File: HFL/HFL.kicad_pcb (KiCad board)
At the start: 2 copper layers, 62.6 x 37.6 mm, 82 parts, among them J1 STS_IO, J2 Conn_01x06_Male, J3 PWR, Q1 2N7002, Q2 MCT06P10-TP, Q3 2N7002, SW1 RST, SW2 BYPASS, U1 74LS32, U2 74LS08, U3 MCP6004, U4 LM1117-5.0, U5 4044, U6 NE555, U7 LTV-817S

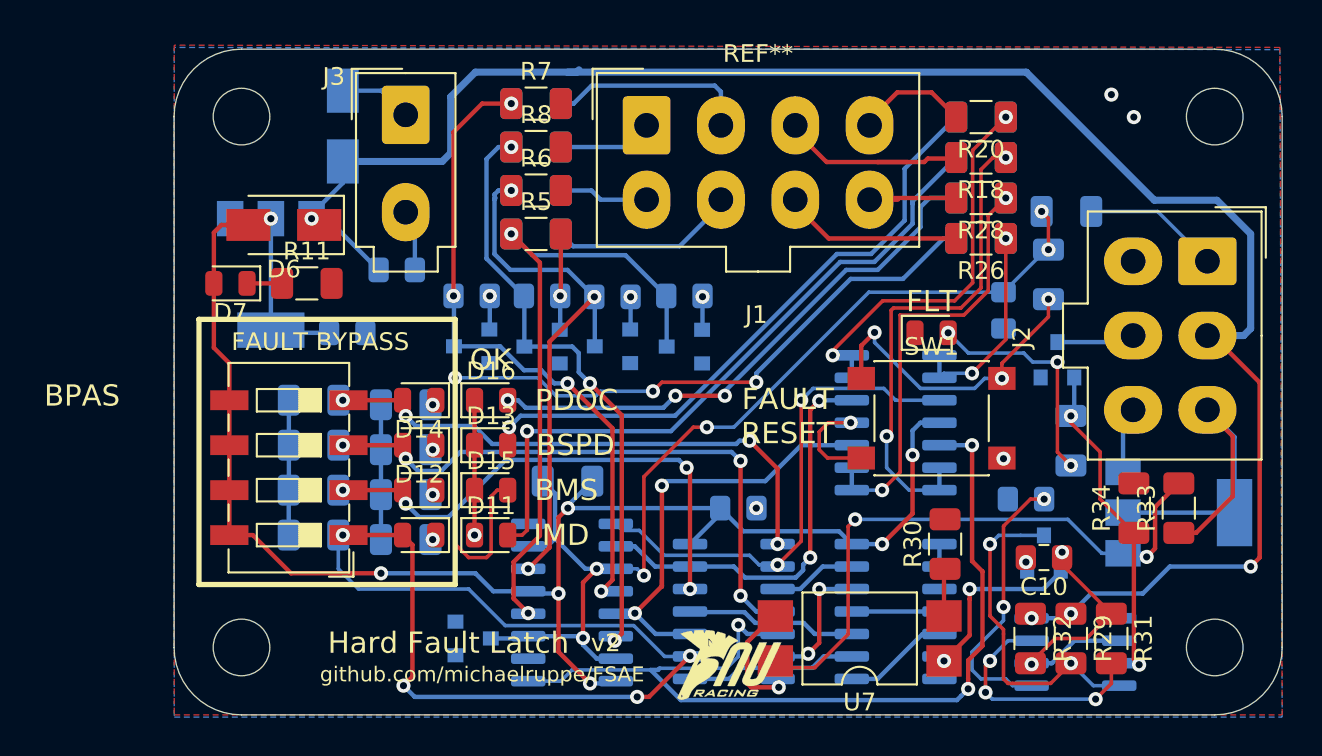
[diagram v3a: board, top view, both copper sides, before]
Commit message: Cosmetic upgrades to HFL v2
also scattered some GND-GND vias
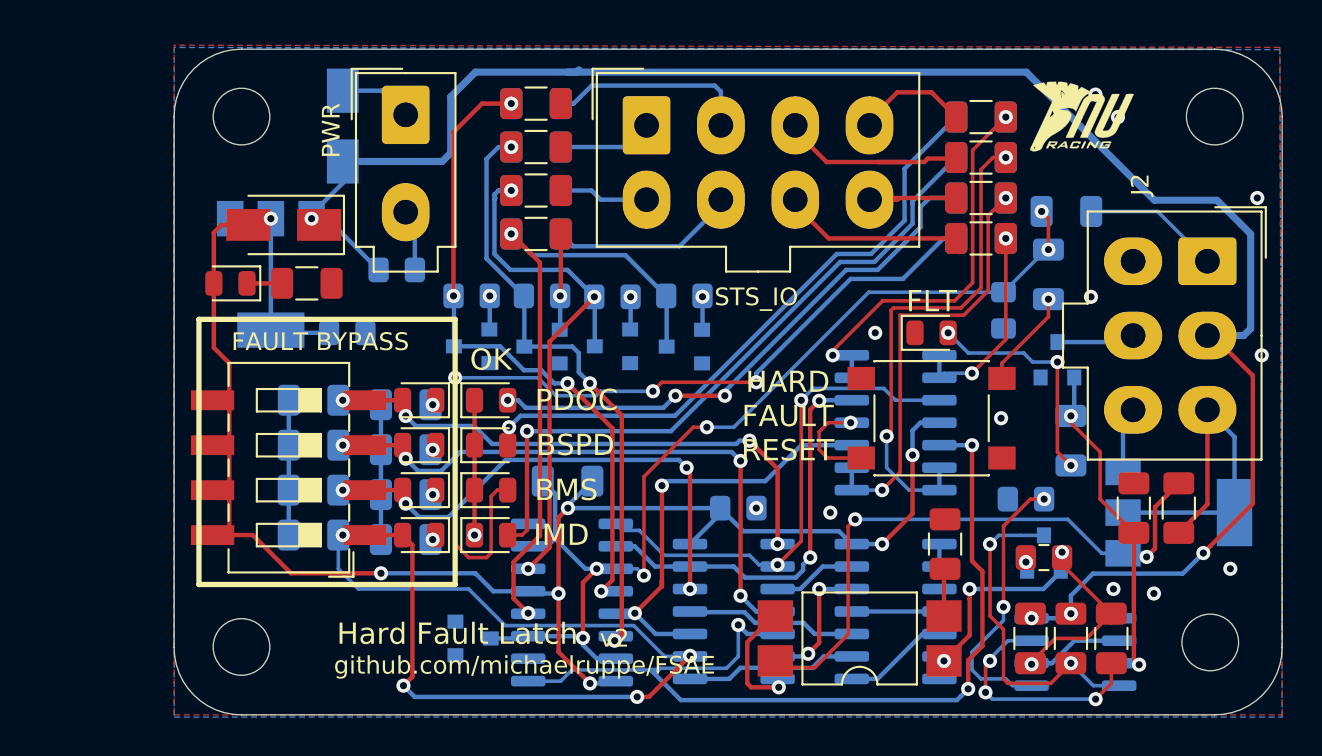
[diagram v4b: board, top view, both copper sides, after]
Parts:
- removed the REF** at (135.0, 79.5)
- removed the REF** at (80.0, 79.5)
- added REF**: MountingHole_3.2mm_M3, MountingHole:MountingHole_3.2mm_M3, F.Cu at (134.8, 79.2)
- added REF**: MountingHole_3.2mm_M3, MountingHole:MountingHole_3.2mm_M3, F.Cu at (80.0, 79.5)
- SW2: footprint Button_Switch_SMD:SW_DIP_SPSTx04_Slide_6.7x11.72mm_W6.73mm_P2.54mm_LowProfile_JPin -> Button_Switch_SMD:SW_DIP_SPSTx04_Slide_6.7x11.72mm_W8.61mm_P2.54mm_LowProfile
- moved G*** 36.8 mm to (127.5, 49.6)
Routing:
- net Net-(R12-Pad2): track 17.6 -> 5.57 mm, vias 3 -> 1
- net SHTDN_IN: track 22.1 -> 20.4 mm
- net +12V: track 105.0 -> 103.3 mm
- net GND: vias 12 -> 20
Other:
- board text added: "HARD FAULT RESET"
- board text added: "PWR"
- board text removed: "BPAS"
- board text removed: "FAULT RESET"

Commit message: Update HFL - pcb silk
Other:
- board text added: "FAULT"
- board text added: "RESET"
- board text removed: "FLT"
- board text removed: "HARD FAULT RESET"

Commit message: Lock down before branch for projects
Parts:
- moved REF** 0.35 mm to (135.0, 79.5)
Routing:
- net +12V: track 103.0 -> 115.4 mm, vias 4 -> 3
- net Net-(Q3-Pad1): track 19.1 -> 20.9 mm
- net GND: vias 20 -> 18
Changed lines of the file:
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@@
     (thickness 1.6)
     (drawings 24)
-    (tracks 655)
+    (tracks 658)
     (zones 0)
     (modules 82)
@@
     (pad_to_mask_clearance 0.051)
     (solder_mask_min_width 0.25)
-    (aux_axis_origin 0 0)
+    (aux_axis_origin 80.01 79.53)
     (grid_origin 80.01 79.53)
     (visible_elements 7FFFFFFF)
@@
     (add_net SHTDN_OUT)
   )
-  (module MountingHole:MountingHole_3.2mm_M3 (layer F.Cu)
-    (at 134.756 79.248)
+  (module MountingHole:MountingHole_3.2mm_M3 locked (layer F.Cu)
+    (at 135 79.502)
     (descr "Mounting Hole 3.2mm, no annular, M3")
     (tags "mounting hole 3.2mm no annular m3")
@@
   )
   (module MountingHole:MountingHole_3.2mm_M3 locked (layer F.Cu)
-    (at 135.01 49.53)
+    (at 135 49.53)
     (descr "Mounting Hole 3.2mm, no annular, M3")
     (tags "mounting hole 3.2mm no annular m3")
@@
   )
   (module MountingHole:MountingHole_3.2mm_M3 locked (layer F.Cu)
-    (at 80.01 49.53)
+    (at 80 49.53)
     (descr "Mounting Hole 3.2mm, no annular, M3")
     (tags "mounting hole 3.2mm no annular m3")
@@
   (via (at 128.016 59.718) (size 0.8) (drill 0.4) (layers F.Cu B.Cu) (net 1))
   (via (at 115.824 61.75) (size 0.8) (drill 0.4) (layers F.Cu B.Cu) (net 1))
-  (via (at 131.572 76.482) (size 0.8) (drill 0.4) (layers F.Cu B.Cu) (net 1))
   (segment (start 115.033 68.826) (end 113.13 68.826) (width 0.2032) (layer F.Cu) (net 1) (status 10))
   (via (at 113.284 71.91) (size 0.8) (drill 0.4) (layers F.Cu B.Cu) (net 1))
-  (via (at 129.286 76.228) (size 0.8) (drill 0.4) (layers F.Cu B.Cu) (net 1))
-  (via (at 135.89 75.085) (size 0.8) (drill 0.4) (layers F.Cu B.Cu) (net 1))
+  (via (at 132.08 76.101) (size 0.8) (drill 0.4) (layers F.Cu B.Cu) (net 1))
   (segment (start 80.3215 58.956) (end 82.302 58.956) (width 0.25) (layer F.Cu) (net 2) (status 30))
   (via (at 90.814 73.434) (size 0.8) (drill 0.4) (layers F.Cu B.Cu) (net 3) (status 30))
@@
   (segment (start 124.661 77.879) (end 126.625 77.879) (width 0.25) (layer B.Cu) (net 4) (status 10))
   (via (at 124.661 77.879) (size 0.8) (drill 0.4) (layers F.Cu B.Cu) (net 4) (status 30))
-  (segment (start 134.765999 73.796001) (end 134.366 74.196) (width 0.25) (layer F.Cu) (net 4))
-  (segment (start 134.596 61.904) (end 134.896 61.904) (width 0.25) (layer F.Cu) (net 4))
+  (segment (start 137.16 64.168) (end 137.16 71.021) (width 0.25) (layer F.Cu) (net 4))
   (segment (start 134.896 61.904) (end 137.16 64.168) (width 0.25) (layer F.Cu) (net 4))
-  (segment (start 137.16 64.168) (end 137.16 71.402) (width 0.25) (layer F.Cu) (net 4))
-  (segment (start 137.16 71.402) (end 134.765999 73.796001) (width 0.25) (layer F.Cu) (net 4))
-  (via (at 134.366 74.196) (size 0.8) (drill 0.4) (layers F.Cu B.Cu) (net 4))
-  (segment (start 133.966001 74.595999) (end 134.366 74.196) (width 0.25) (layer B.Cu) (net 4))
-  (segment (start 133.204001 75.357999) (end 133.966001 74.595999) (width 0.25) (layer B.Cu) (net 4))
-  (segment (start 128.124001 75.357999) (end 133.204001 75.357999) (width 0.25) (layer B.Cu) (net 4))
-  (segment (start 126.882 77.622) (end 126.882 76.6) (width 0.25) (layer B.Cu) (net 4))
-  (segment (start 126.882 76.6) (end 128.124001 75.357999) (width 0.25) (layer B.Cu) (net 4))
+  (segment (start 134.596 61.904) (end 134.896 61.904) (width 0.25) (layer F.Cu) (net 4))
+  (segment (start 137.795 64.803) (end 134.896 61.904) (width 0.25) (layer B.Cu) (net 4))
+  (segment (start 128.784 75.72) (end 130.937 75.72) (width 0.25) (layer B.Cu) (net 4))
+  (segment (start 126.882 77.622) (end 128.784 75.72) (width 0.25) (layer B.Cu) (net 4))
+  (segment (start 134.896 61.904) (end 134.596 61.904) (width 0.25) (layer B.Cu) (net 4))
+  (segment (start 130.937 75.72) (end 131.953 74.704) (width 0.25) (layer B.Cu) (net 4))
+  (segment (start 131.953 74.704) (end 137.432999 74.704) (width 0.25) (layer B.Cu) (net 4))
+  (segment (start 137.432999 74.704) (end 137.795 74.341999) (width 0.25) (layer B.Cu) (net 4))
+  (segment (start 137.795 74.341999) (end 137.795 64.803) (width 0.25) (layer B.Cu) (net 4))
   (via (at 95.256 56.162) (size 0.8) (drill 0.4) (layers F.Cu B.Cu) (net 5) (status 30))
   (segment (start 104.038 59.689666) (end 104.013 59.664666) (width 0.25) (layer B.Cu) (net 5) (status 30))
@@
   (via (at 90.814 68.354) (size 0.8) (drill 0.4) (layers F.Cu B.Cu) (net 39) (status 30))
   (via (at 90.814 65.814) (size 0.8) (drill 0.4) (layers F.Cu B.Cu) (net 40) (status 30))
-  (via (at 131.16301 74.412988) (size 0.8) (drill 0.4) (layers F.Cu B.Cu) (net 41))
-  (segment (start 132.978 70.256) (end 131.63801 71.59599) (width 0.25) (layer F.Cu) (net 41) (status 10))
-  (segment (start 131.63801 71.59599) (end 131.63801 73.937988) (width 0.25) (layer F.Cu) (net 41))
-  (segment (start 131.63801 73.937988) (end 131.16301 74.412988) (width 0.25) (layer F.Cu) (net 41))
   (segment (start 128.6248 74.21) (end 126.7058 72.291) (width 0.2032) (layer B.Cu) (net 41))
   (segment (start 129.828 74.21) (end 128.6248 74.21) (width 0.2032) (layer B.Cu) (net 41) (status 10))
@@
   (segment (start 114.69 72.291) (end 114.290001 72.690999) (width 0.2032) (layer F.Cu) (net 41))
   (segment (start 114.290001 72.690999) (end 114.290001 78.786999) (width 0.2032) (layer F.Cu) (net 41))
-  (segment (start 130.960022 74.21) (end 131.16301 74.412988) (width 0.2032) (layer B.Cu) (net 41))
-  (segment (start 129.828 74.21) (end 130.960022 74.21) (width 0.2032) (layer B.Cu) (net 41) (status 10))
+  (segment (start 129.828 74.21) (end 129.860999 74.177001) (width 0.2032) (layer B.Cu) (net 41))
+  (segment (start 132.978 70.256) (end 131.699 71.535) (width 0.25) (layer F.Cu) (net 41))
+  (segment (start 129.860999 74.177001) (end 129.902001 74.177001) (width 0.2032) (layer B.Cu) (net 41))
+  (segment (start 129.902001 74.177001) (end 130.302 74.577) (width 0.2032) (layer B.Cu) (net 41))
+  (segment (start 130.867685 74.577) (end 130.302 74.577) (width 0.25) (layer F.Cu) (net 41))
+  (segment (start 131.699 73.745685) (end 130.867685 74.577) (width 0.25) (layer F.Cu) (net 41))
+  (via (at 130.302 74.577) (size 0.8) (drill 0.4) (layers F.Cu B.Cu) (net 41))
+  (segment (start 131.699 71.535) (end 131.699 73.745685) (width 0.25) (layer F.Cu) (net 41))
   (segment (start 127.07 66.258) (end 126.882 66.446) (width 0.25) (layer B.Cu) (net 42) (status 30))
   (segment (start 127.07 64.274) (end 127.07 66.258) (width 0.25) (layer B.Cu) (net 42) (status 30))
@@
   (segment (start 128.533 68.481) (end 126.882 66.83) (width 0.2032) (layer F.Cu) (net 42))
   (segment (start 126.882 66.83) (end 126.882 66.446) (width 0.2032) (layer F.Cu) (net 42))
-  (segment (start 130.438 73.056) (end 130.438 80.20591) (width 0.25) (layer F.Cu) (net 42) (status 10))
   (via (at 130.736824 80.504734) (size 0.8) (drill 0.4) (layers F.Cu B.Cu) (net 42))
-  (segment (start 130.438 80.20591) (end 130.736824 80.504734) (width 0.25) (layer F.Cu) (net 42))
   (segment (start 129.696734 80.504734) (end 129.611 80.419) (width 0.25) (layer B.Cu) (net 42) (status 30))
   (segment (start 130.736824 80.504734) (end 129.696734 80.504734) (width 0.25) (layer B.Cu) (net 42) (status 20))
+  (segment (start 130.736824 80.504734) (end 130.736824 76.465826) (width 0.25) (layer F.Cu) (net 42))
+  (segment (start 128.905 73.614) (end 129.463 73.056) (width 0.25) (layer F.Cu) (net 42))
+  (segment (start 129.463 73.056) (end 130.438 73.056) (width 0.25) (layer F.Cu) (net 42))
+  (segment (start 128.905 74.634002) (end 128.905 73.614) (width 0.25) (layer F.Cu) (net 42))
+  (segment (start 130.736824 76.465826) (end 128.905 74.634002) (width 0.25) (layer F.Cu) (net 42))
   (via (at 125.612 59.848) (size 0.8) (drill 0.4) (layers F.Cu B.Cu) (net 43) (status 30))
   (segment (start 125.612 60.8438) (end 125.612 59.848) (width 0.2032) (layer F.Cu) (net 43))
